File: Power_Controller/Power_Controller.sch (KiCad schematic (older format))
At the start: 23 parts, among them J1 CONN_01X04_MALE, Q1 CSD16570Q5B, SW1 SW_Push, U1 MIC5060, U2 FAN4010, U3 STM32L021D4P6, U4 MPM3620A, U5 TCR2LE33LM

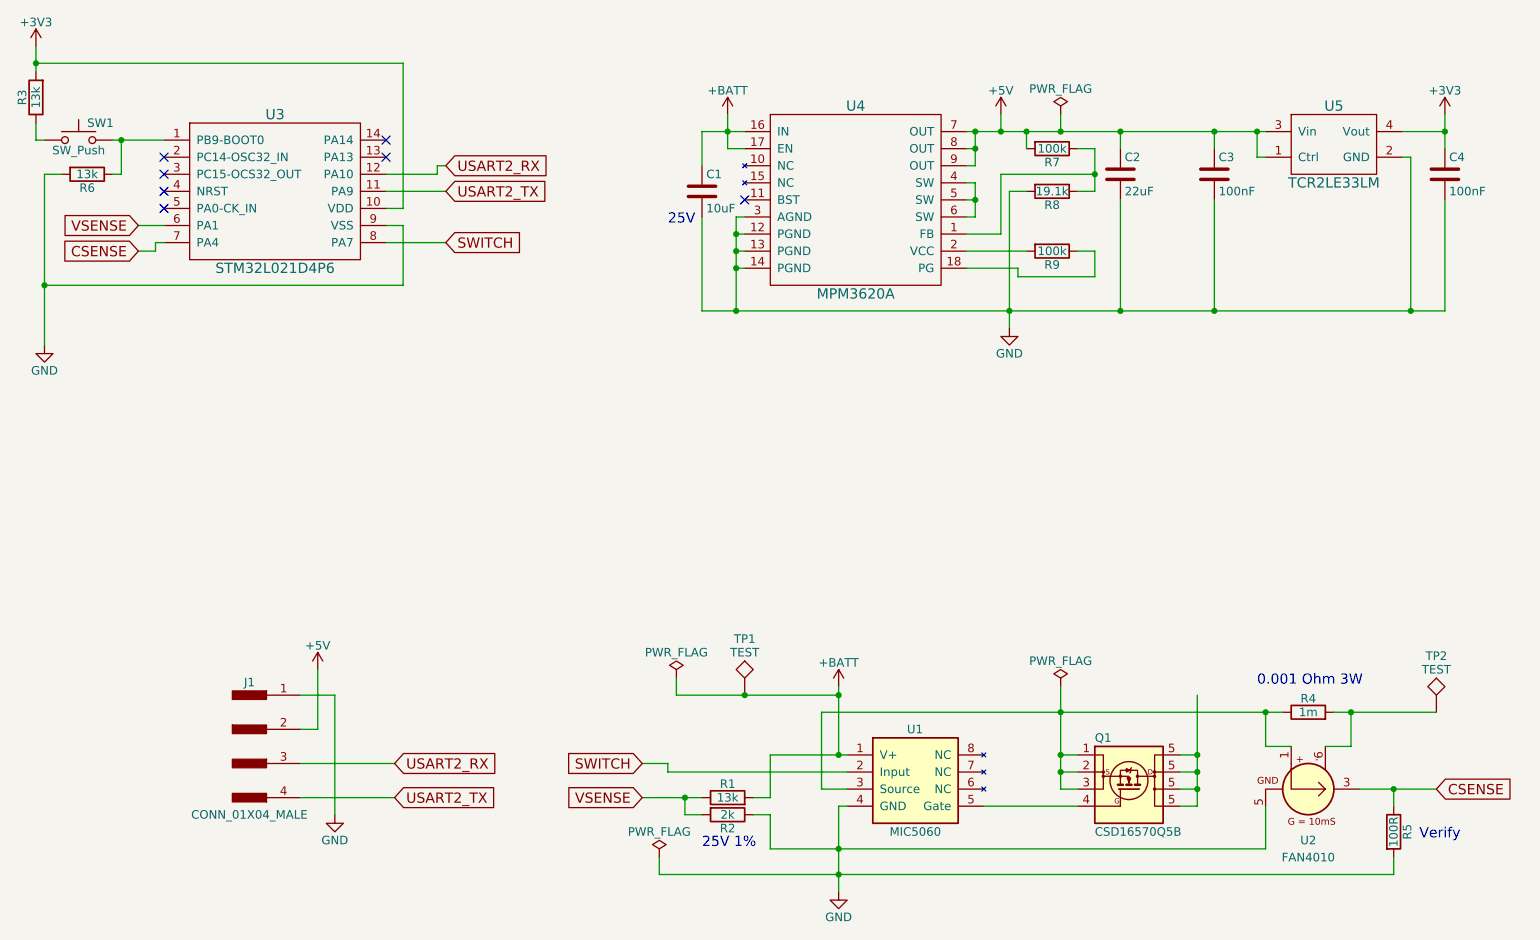
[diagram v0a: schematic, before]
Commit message: V1.0 of the power controller, using the LTC2946
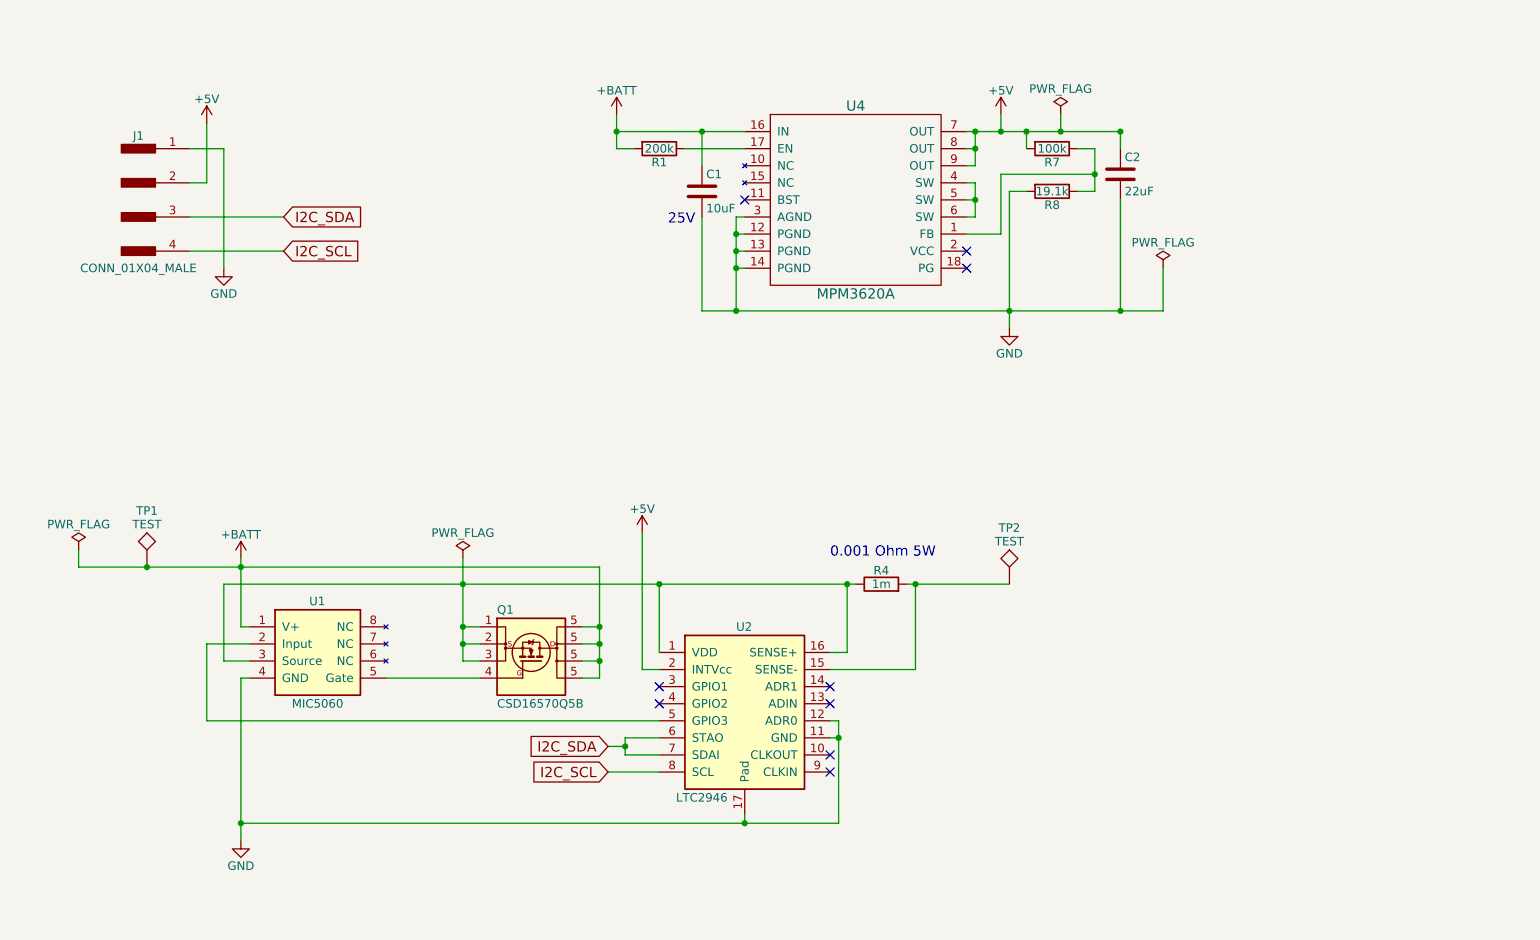
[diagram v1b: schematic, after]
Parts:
- removed C3, C4: 100nF, Capacitors_SMD:C_0402, symbol C
- removed R2: 2k, Resistors_SMD:R_0402, symbol R
- removed R3, R6: 13k, Resistors_SMD:R_0402, symbol R
- removed R5: 100R, Resistors_SMD:R_0402, symbol R
- removed R9: 100k, Resistors_SMD:R_0402, symbol R
- removed SW1: SW_Push, jumper:SOLDER-JUMPER_1-WAY, symbol SW_Push
- removed U2: FAN4010, local:FAIRCHILD-MLP-6, symbol FAN4010
- removed U3: STM32L021D4P6, local:TSSOP14, symbol STM32L021D4P6
- removed U5: TCR2LE33LM, TO_SOT_Packages_SMD:SOT-553, symbol TCR2LE33LM
- added U2: LTC2946, local:LTC2946, symbol LTC2946
- R1: value 13k -> 200k
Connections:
- net +5V: now also U2.2 (INTVcc)
- net +BATT: now also Q1.5 (D); no longer U4.17 (EN)
- net GND: now also U2.11 (GND), U2.12 (ADR0), U2.17 (Pad)
- net at Q1.1 (S), Q1.2 (S), Q1.3 (S)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: now also U2.1 (VDD), U2.16 (SENSE+)
- net at R4.2, TP2.1: now also U2.15 (SENSE-)
- net SWITCH: no longer names the net of U1.2 (Input)
- net SWITCH: now also U2.5 (GPIO3)
- net USART2_RX renamed I2C_SDA
- net I2C_SDA: now also U2.6 (STAO), U2.7 (SDAI)
- net USART2_TX renamed I2C_SCL
- net I2C_SCL: now also U2.8 (SCL)
- net VSENSE: no longer names the net of R1.1
- net VSENSE: now also U4.17 (EN)
- no-connect marks 7 -> 9
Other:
- note added: "0.001 Ohm 5W"
- note removed: "0.001 Ohm 3W"
- note removed: "25V 1%"
- note removed: "Verify"
- moved on the sheet: J1, Q1, R4, TP1, TP2, U1

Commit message: Updates GPS Diamond to 1.1.
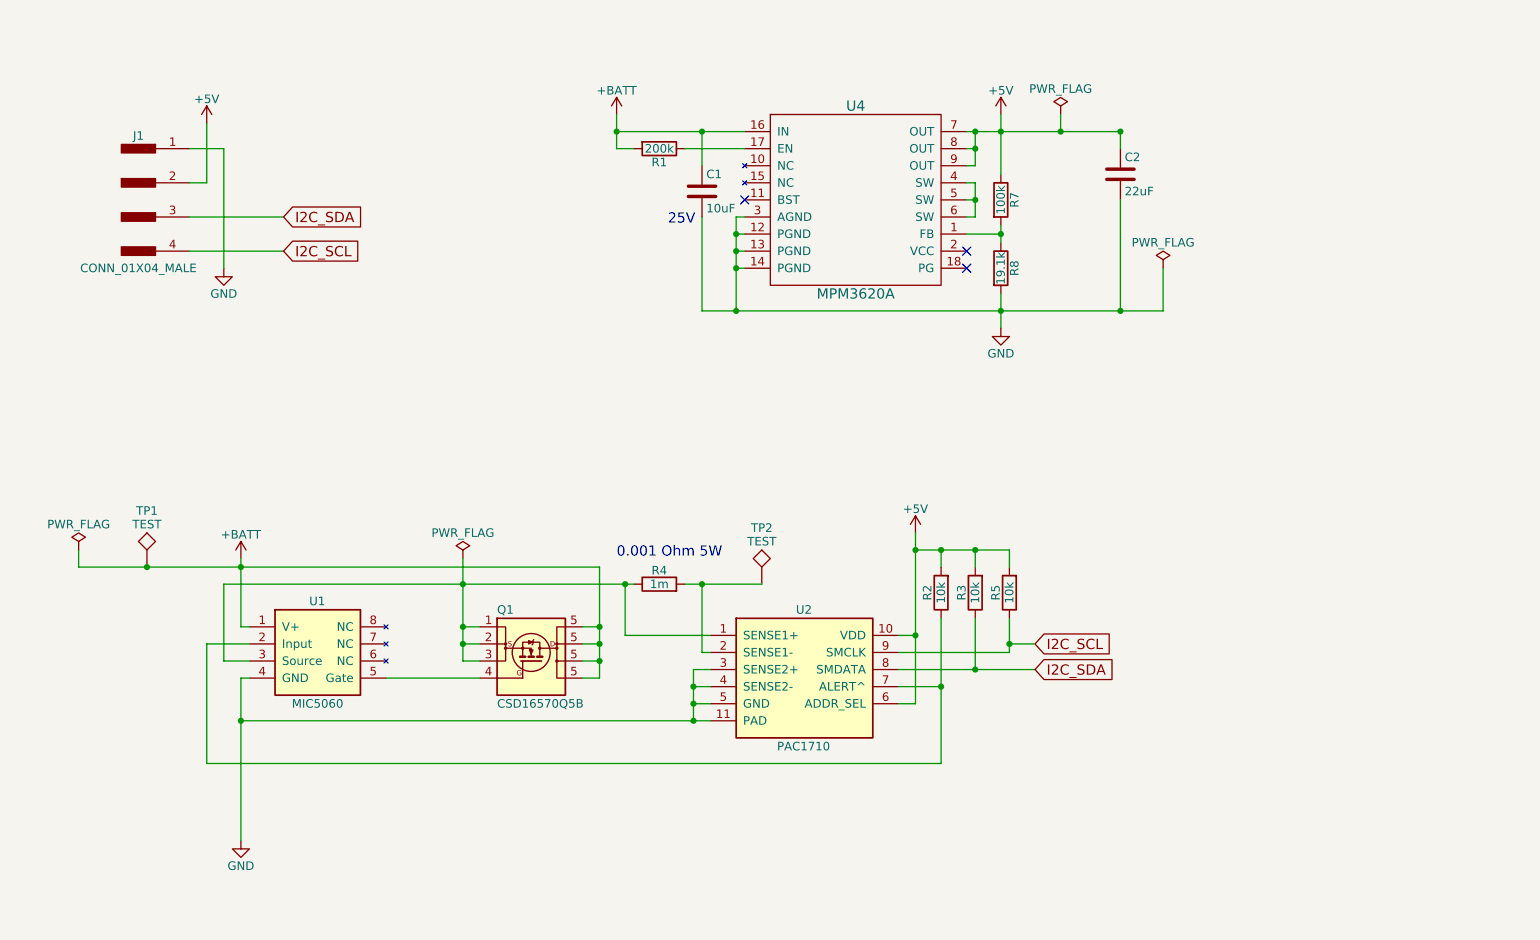
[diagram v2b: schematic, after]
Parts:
- removed U2: LTC2946, local:LTC2946, symbol LTC2946
- added R2, R3, R5: 10k, Resistors_SMD:R_0402, symbol R
- added U2: PAC1710, local:PAC1720, symbol PAC1710
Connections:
- net +5V: now also R7.1, R2.2, R3.2, R5.2, U2.10 (VDD), U2.6 (ADDR_SEL); no longer R7.2
- net GND: now also U2.11 (PAD), U2.3 (SENSE2+), U2.4 (SENSE2-), U2.5 (GND)
- net I2C_SCL: now also R5.1, U2.9 (SMCLK)
- net I2C_SDA: now also R3.1, U2.8 (SMDATA)
- net at Q1.1 (S), Q1.2 (S), Q1.3 (S)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: now also U2.1 (SENSE1+)
- net at U1.2 (Input): now also R2.1, U2.7 (ALERT^)
- net at R4.2, TP2.1: now also U2.2 (SENSE1-)
- net at R8.1, U4.1 (FB): now also R7.2; no longer R7.1
- no-connect marks 9 -> 3
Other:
- moved on the sheet: R4, R7, R8, TP2
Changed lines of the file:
@@
 L R R4
 U 1 1 59055480
-P 6450 4450
-F 0 "R4" V 6530 4450 50  0000 C CNN
-F 1 "1m" V 6450 4450 50  0000 C CNN
-F 2 "Resistors_SMD:R_2512" V 6380 4450 50  0001 C CNN
-F 3 "" H 6450 4450 50  0001 C CNN
-	1    6450 4450
+P 5150 4450
+F 0 "R4" V 5230 4450 50  0000 C CNN
+F 1 "1m" V 5150 4450 50  0000 C CNN
+F 2 "Resistors_SMD:R_2512" V 5080 4450 50  0001 C CNN
+F 3 "" H 5150 4450 50  0001 C CNN
+	1    5150 4450
 	0    -1   -1   0
 $EndComp
-Text Notes 6150 4300 0    60   ~ 0
+Text Notes 4900 4300 0    60   ~ 0
 0.001 Ohm 5W
 $Comp
@@
 L TEST TP2
 U 1 1 59055FFF
-P 7200 4450
-F 0 "TP2" H 7200 4750 50  0000 C BNN
-F 1 "TEST" H 7200 4700 50  0000 C CNN
-F 2 "local:SMD_Battery_Pad" H 7200 4450 50  0001 C CNN
-F 3 "" H 7200 4450 50  0001 C CNN
-	1    7200 4450
+P 5750 4450
+F 0 "TP2" H 5750 4750 50  0000 C BNN
+F 1 "TEST" H 5750 4700 50  0000 C CNN
+F 2 "local:SMD_Battery_Pad" H 5750 4450 50  0001 C CNN
+F 3 "" H 5750 4450 50  0001 C CNN
+	1    5750 4450
 	1    0    0    -1
 $EndComp
@@
 L R R7
 U 1 1 5909664F
-P 7450 1900
-F 0 "R7" V 7530 1900 50  0000 C CNN
-F 1 "100k" V 7450 1900 50  0000 C CNN
-F 2 "Resistors_SMD:R_0402" V 7380 1900 50  0001 C CNN
-F 3 "" H 7450 1900 50  0001 C CNN
-	1    7450 1900
-	0    1    1    0
+P 7150 2200
+F 0 "R7" V 7230 2200 50  0000 C CNN
+F 1 "100k" V 7150 2200 50  0000 C CNN
+F 2 "Resistors_SMD:R_0402" V 7080 2200 50  0001 C CNN
+F 3 "" H 7150 2200 50  0001 C CNN
+	1    7150 2200
+	1    0    0    -1
 $EndComp
 $Comp
 L R R8
 U 1 1 590966F8
-P 7450 2150
-F 0 "R8" V 7530 2150 50  0000 C CNN
-F 1 "19.1k" V 7450 2150 50  0000 C CNN
-F 2 "Resistors_SMD:R_0402" V 7380 2150 50  0001 C CNN
-F 3 "" H 7450 2150 50  0001 C CNN
-	1    7450 2150
-	0    1    1    0
+P 7150 2600
+F 0 "R8" V 7230 2600 50  0000 C CNN
+F 1 "19.1k" V 7150 2600 50  0000 C CNN
+F 2 "Resistors_SMD:R_0402" V 7080 2600 50  0001 C CNN
+F 3 "" H 7150 2600 50  0001 C CNN
+	1    7150 2600
+	1    0    0    -1
 $EndComp
 $Comp
@@
 L GND #PWR09
 U 1 1 59097364
-P 7200 2950
-F 0 "#PWR09" H 7200 2700 50  0001 C CNN
-F 1 "GND" H 7200 2800 50  0000 C CNN
-F 2 "" H 7200 2950 50  0001 C CNN
-F 3 "" H 7200 2950 50  0001 C CNN
-	1    7200 2950
+P 7150 2950
+F 0 "#PWR09" H 7150 2700 50  0001 C CNN
+F 1 "GND" H 7150 2800 50  0000 C CNN
+F 2 "" H 7150 2950 50  0001 C CNN
+F 3 "" H 7150 2950 50  0001 C CNN
+	1    7150 2950
 	1    0    0    -1
 $EndComp
@@
 Connection ~ 4800 4900
 Wire Wire Line
-	6600 4450 7200 4450
+	5300 4450 5750 4450
 Wire Wire Line
 	2400 1900 2600 1900
@@
 Connection ~ 2150 4350
 Wire Wire Line
-	2600 4450 6300 4450
+	2600 4450 5000 4450
 Connection ~ 4000 4450
 Wire Wire Line
@@
 	2500 2100 2500 1750
 Wire Wire Line
-	7150 1800 7150 1700
-Wire Wire Line
-	7300 1800 7300 1900
+	7150 1700 7150 2050
 Connection ~ 7150 1800
-Wire Wire Line
-	7600 1900 7700 1900
-Wire Wire Line
-	7700 1900 7700 2150
-Wire Wire Line
-	7700 2150 7600 2150
 Wire Wire Line
 	7000 2300 6950 2300
@@
 Connection ~ 7000 2200
 Wire Wire Line
-	7300 2150 7200 2150
-Wire Wire Line
-	7200 2150 7200 2950
-Wire Wire Line
 	7000 2000 6950 2000
 Wire Wire Line
@@
 Connection ~ 7000 1900
 Wire Wire Line
-	6950 2400 7150 2400
-Wire Wire Line
-	7150 2400 7150 2050
-Wire Wire Line
-	7150 2050 7700 2050
-Connection ~ 7700 2050
-Wire Wire Line
 	5600 2600 5650 2600
 Wire Wire Line
 	5600 2300 5600 2850
-Connection ~ 7200 2850
 Wire Wire Line
 	5650 2300 5600 2300
@@
 Wire Wire Line
 	7850 1800 7850 1900
-Connection ~ 7300 1800
 Wire Wire Line
 	7850 2850 7850 2200
@@
 Connection ~ 7850 2850
 $Comp
-L LTC2946 U2
-U 1 1 590A8ED2
-P 5650 5200
-F 0 "U2" H 5600 5700 50  0000 L CNN
-F 1 "LTC2946" H 5550 4700 50  0000 R CNN
-F 2 "local:LTC2946" H 6000 4700 50  0001 C CIN
-F 3 "" H 5650 5200 50  0000 C CNN
-	1    5650 5200
-	1    0    0    -1
-$EndComp
-$Comp
 L +5V #PWR012
 U 1 1 590A90AE
-P 5050 4150
-F 0 "#PWR012" H 5050 4000 50  0001 C CNN
-F 1 "+5V" H 5050 4290 50  0000 C CNN
-F 2 "" H 5050 4150 50  0001 C CNN
-F 3 "" H 5050 4150 50  0001 C CNN
-	1    5050 4150
-	1    0    0    -1
-$EndComp
-Wire Wire Line
-	6150 4850 6250 4850
-Wire Wire Line
-	6250 4850 6250 4450
-Connection ~ 6250 4450
-Wire Wire Line
-	6150 4950 6650 4950
-Wire Wire Line
-	6650 4950 6650 4450
-Connection ~ 6650 4450
-NoConn ~ 5150 5050
-NoConn ~ 5150 5150
-Wire Wire Line
-	5150 5250 2500 5250
-Wire Wire Line
-	2500 5250 2500 4800
+P 6650 4150
+F 0 "#PWR012" H 6650 4000 50  0001 C CNN
+F 1 "+5V" H 6650 4290 50  0000 C CNN
+F 2 "" H 6650 4150 50  0001 C CNN
+F 3 "" H 6650 4150 50  0001 C CNN
+	1    6650 4150
+	1    0    0    -1
+$EndComp
 Wire Wire Line
 	2500 4800 2750 4800
-NoConn ~ 6150 5150
-Text GLabel 4850 5400 0    60   Input ~ 0
+Text GLabel 7350 4950 2    60   Input ~ 0
 I2C_SDA
-Text GLabel 4850 5550 0    60   Input ~ 0
+Text GLabel 7350 4800 2    60   Input ~ 0
 I2C_SCL
-Wire Wire Line
-	4850 5550 5150 5550
-Wire Wire Line
-	4950 5450 5150 5450
-Wire Wire Line
-	4950 5350 4950 5450
-Wire Wire Line
-	4950 5400 4850 5400
-Wire Wire Line
-	5150 5350 4950 5350
-Connection ~ 4950 5400
-NoConn ~ 6150 5450
-NoConn ~ 6150 5550
-Wire Wire Line
-	6150 5350 6200 5350
-Wire Wire Line
-	6200 5850 6200 5250
-Wire Wire Line
-	6200 5250 6150 5250
-Connection ~ 6200 5350
-NoConn ~ 6150 5050
-Wire Wire Line
-	5150 4950 5050 4950
-Wire Wire Line
-	5050 4950 5050 4150
-Wire Wire Line
-	5150 4850 5150 4450
-Connection ~ 5150 4450
 Text GLabel 2950 2300 2    60   Input ~ 0
 I2C_SDA
-Wire Wire Line
-	2700 5850 6200 5850
-Wire Wire Line
-	5650 5850 5650 5800
-Connection ~ 2700 5850
-Connection ~ 5650 5850
 NoConn ~ 6950 2500
 NoConn ~ 6950 2600
@@
 	5650 1900 5300 1900
 Wire Wire Line
-	5000 1900 4900 1900
-Wire Wire Line
-	4900 1900 4900 1700
+	4900 1900 5000 1900
+Wire Wire Line
+	4900 1700 4900 1900
 Connection ~ 4900 1800
 Connection ~ 5400 1800
+$Comp
+L PAC1710 U2
+U 1 1 591A4998
+P 6000 5000
+F 0 "U2" H 5950 5400 50  0000 L CNN
+F 1 "PAC1710" H 6150 4600 50  0000 R CNN
+F 2 "local:PAC1720" H 6000 4500 50  0001 C CIN
+F 3 "" H 6000 5000 50  0000 C CNN
+	1    6000 5000
+	1    0    0    -1
+$EndComp
+Wire Wire Line
+	5450 4750 4950 4750
+Wire Wire Line
+	4950 4750 4950 4450
+Connection ~ 4950 4450
+Wire Wire Line
+	5450 4850 5400 4850
+Wire Wire Line
+	5400 4850 5400 4450
+Connection ~ 5400 4450
+Wire Wire Line
+	2700 5250 5450 5250
+Connection ~ 2700 5250
+Wire Wire Line
+	5350 5150 5450 5150
+Wire Wire Line
+	5350 4950 5350 5250
+Connection ~ 5350 5250
+Wire Wire Line
+	5450 5050 5350 5050
+Connection ~ 5350 5150
+Wire Wire Line
+	5450 4950 5350 4950
+Connection ~ 5350 5050
+Wire Wire Line
+	6550 4750 6650 4750
+Wire Wire Line
+	6650 4150 6650 5150
+Wire Wire Line
+	7150 2350 7150 2450
+Wire Wire Line
+	7150 2750 7150 2950
+Connection ~ 7150 2850
+Wire Wire Line
+	6950 2400 7150 2400
+Connection ~ 7150 2400
+$Comp
+L R R2
+U 1 1 591A59F2
+P 6800 4500
+F 0 "R2" V 6880 4500 50  0000 C CNN
+F 1 "10k" V 6800 4500 50  0000 C CNN
+F 2 "Resistors_SMD:R_0402" V 6730 4500 50  0001 C CNN
+F 3 "" H 6800 4500 50  0001 C CNN
+	1    6800 4500
+	-1   0    0    1
+$EndComp
+$Comp
+L R R3
+U 1 1 591A5CBC
+P 7000 4500
+F 0 "R3" V 7080 4500 50  0000 C CNN
+F 1 "10k" V 7000 4500 50  0000 C CNN
+F 2 "Resistors_SMD:R_0402" V 6930 4500 50  0001 C CNN
+F 3 "" H 7000 4500 50  0001 C CNN
+	1    7000 4500
+	-1   0    0    1
+$EndComp
+$Comp
+L R R5
+U 1 1 591A5D05
+P 7200 4500
+F 0 "R5" V 7280 4500 50  0000 C CNN
+F 1 "10k" V 7200 4500 50  0000 C CNN
+F 2 "Resistors_SMD:R_0402" V 7130 4500 50  0001 C CNN
+F 3 "" H 7200 4500 50  0001 C CNN
+	1    7200 4500
+	-1   0    0    1
+$EndComp
+Wire Wire Line
+	6800 4650 6800 5500
+Wire Wire Line
+	6800 5050 6550 5050
+Wire Wire Line
+	6550 4850 7200 4850
+Wire Wire Line
+	7200 4850 7200 4650
+Wire Wire Line
+	7350 4800 7200 4800
+Connection ~ 7200 4800
+Wire Wire Line
+	6550 4950 7350 4950
+Wire Wire Line
+	7000 4650 7000 4950
+Connection ~ 7000 4950
+Wire Wire Line
+	7200 4350 7200 4250
+Wire Wire Line
+	7200 4250 6650 4250
+Connection ~ 6650 4250
+Wire Wire Line
+	6800 4350 6800 4250
+Connection ~ 6800 4250
+Wire Wire Line
+	7000 4350 7000 4250
+Connection ~ 7000 4250
+Wire Wire Line
+	2500 4800 2500 5500
+Wire Wire Line
+	2500 5500 6800 5500
+Connection ~ 6800 5050
+Wire Wire Line
+	6650 5150 6550 5150
+Connection ~ 6650 4750
 $EndSCHEMATC
